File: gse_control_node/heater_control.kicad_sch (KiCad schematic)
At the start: 2 parts, among them J11 Conn_02x02_Counter_Clockwise, J12 Conn_02x04_Counter_Clockwise

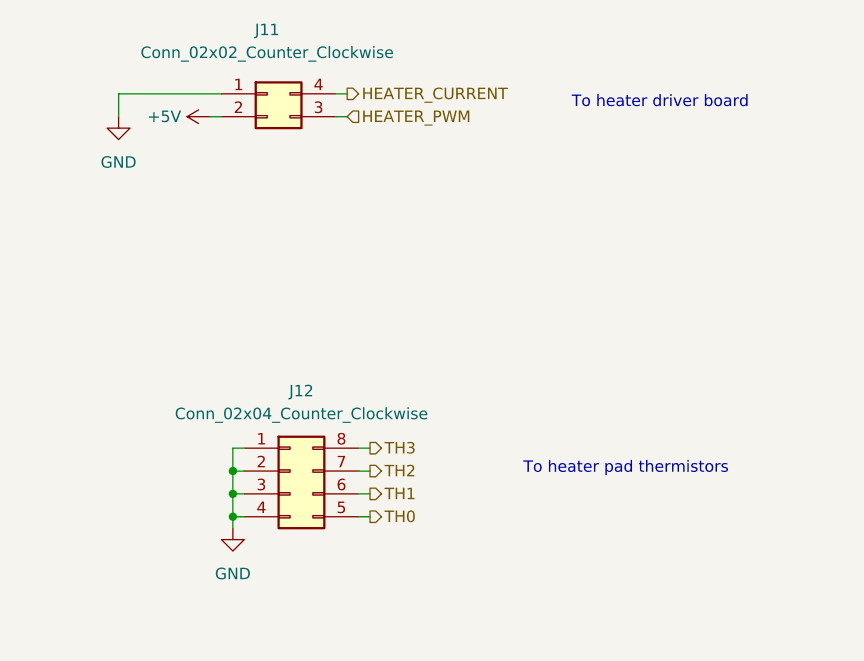
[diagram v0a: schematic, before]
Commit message: finish control board routing
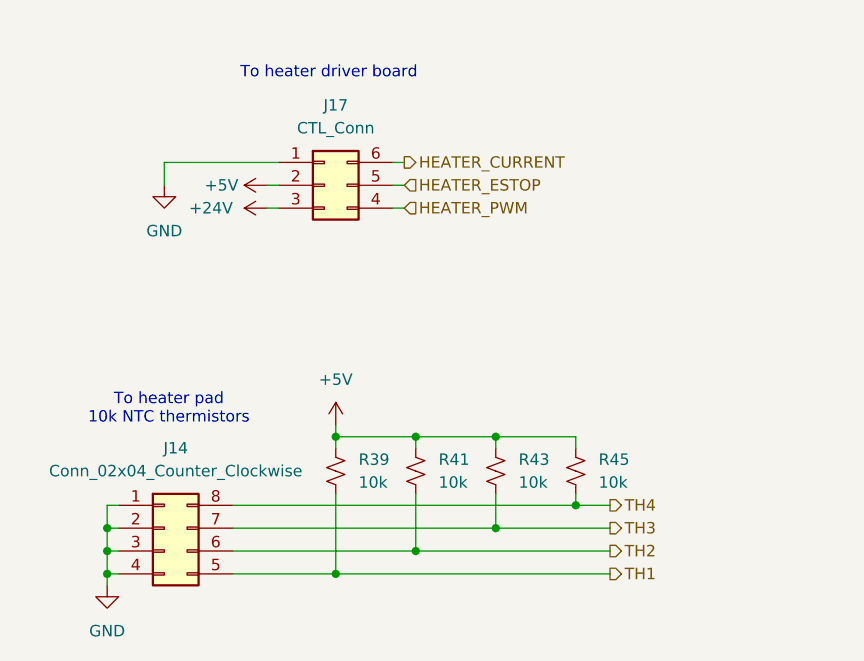
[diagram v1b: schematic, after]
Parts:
- removed J11: Conn_02x02_Counter_Clockwise, Connector_Molex:Molex_Micro-Fit_3.0_43045-0412_2x02_P3.00mm_Vertical, symbol Connector_Generic:Conn_02x02_Counter_Clockwise
- added J17: CTL_Conn, Connector_Molex:Molex_Micro-Fit_3.0_43045-0612_2x03_P3.00mm_Vertical, symbol Connector_Generic:Conn_02x03_Counter_Clockwise
- added R39, R41, R43, R45: 10k, Resistor_SMD:R_0603_1608Metric, symbol Device:R_Small_US
- renumbered J12 to J14
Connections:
- net TH0 is gone; now on net TH1: J14.5 (Pin_5)
- net +5V: now also J17.2 (Pin_2), R39.1, R41.1, R43.1, R45.1
- net GND: now also J17.1 (Pin_1)
- net HEATER_CURRENT: now also J17.6 (Pin_6)
- net HEATER_PWM: now also J17.4 (Pin_4)
- net TH1: now also R39.2; no longer J14.6 (Pin_6)
- net TH2: now also J14.6 (Pin_6), R41.2; no longer J14.7 (Pin_7)
- net TH3: now also J14.7 (Pin_7), R43.2; no longer J14.8 (Pin_8)
- new net +24V: J17.3 (Pin_3)
- new net HEATER_ESTOP: J17.5 (Pin_5)
- new net TH4: J14.8 (Pin_8), R45.2
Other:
- note added: "To heater pad 10k NTC thermistors"
- note removed: "To heater pad thermistors"
- moved on the sheet: J14

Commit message: updates for manufacturing
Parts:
- R39, R41, R43, R45: value 10k -> 10k 0.1%
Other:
- moved on the sheet: R41, R43, R45
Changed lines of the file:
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@@
+	)
+	(junction
+		(at 135.89 129.54)
+		(diameter 0)
+		(color 0 0 0 0)
 	)
 	(junction
@@
 	)
 	(junction
-		(at 153.67 124.46)
-		(diameter 0)
-		(color 0 0 0 0)
-	)
-	(junction
-		(at 144.78 127)
+		(at 148.59 127)
 		(diameter 0)
 		(color 0 0 0 0)
@@
 	)
 	(junction
-		(at 153.67 114.3)
-		(diameter 0)
-		(color 0 0 0 0)
-	)
-	(junction
-		(at 162.56 121.92)
+		(at 161.29 124.46)
 		(diameter 0)
 		(color 0 0 0 0)
@@
 	)
 	(junction
-		(at 144.78 114.3)
-		(diameter 0)
-		(color 0 0 0 0)
-	)
-	(junction
-		(at 135.89 129.54)
-		(diameter 0)
-		(color 0 0 0 0)
-	)
-	(junction
 		(at 110.49 124.46)
 		(diameter 0)
 		(color 0 0 0 0)
 	)
-	(wire
-		(pts
-			(xy 144.78 120.65) (xy 144.78 127)
-		)
-		(stroke
-			(width 0)
-			(type default)
-		)
-	)
-	(wire
-		(pts
-			(xy 162.56 121.92) (xy 166.37 121.92)
+	(junction
+		(at 173.99 121.92)
+		(diameter 0)
+		(color 0 0 0 0)
+	)
+	(junction
+		(at 161.29 114.3)
+		(diameter 0)
+		(color 0 0 0 0)
+	)
+	(junction
+		(at 148.59 114.3)
+		(diameter 0)
+		(color 0 0 0 0)
+	)
+	(wire
+		(pts
+			(xy 148.59 120.65) (xy 148.59 127)
 		)
 		(stroke
@@
 	(wire
 		(pts
-			(xy 153.67 124.46) (xy 166.37 124.46)
-		)
-		(stroke
-			(width 0)
-			(type default)
-		)
-	)
-	(wire
-		(pts
 			(xy 110.49 124.46) (xy 110.49 121.92)
 		)
@@
 	(wire
 		(pts
-			(xy 153.67 114.3) (xy 144.78 114.3)
+			(xy 148.59 114.3) (xy 161.29 114.3)
 		)
 		(stroke
@@
 	(wire
 		(pts
-			(xy 124.46 127) (xy 144.78 127)
-		)
-		(stroke
-			(width 0)
-			(type default)
-		)
-	)
-	(wire
-		(pts
-			(xy 162.56 115.57) (xy 162.56 114.3)
+			(xy 124.46 127) (xy 148.59 127)
+		)
+		(stroke
+			(width 0)
+			(type default)
+		)
+	)
+	(wire
+		(pts
+			(xy 173.99 115.57) (xy 173.99 114.3)
 		)
 		(stroke
@@
 	(wire
 		(pts
-			(xy 162.56 120.65) (xy 162.56 121.92)
+			(xy 173.99 120.65) (xy 173.99 121.92)
 		)
 		(stroke
@@
 	(wire
 		(pts
-			(xy 124.46 124.46) (xy 153.67 124.46)
+			(xy 173.99 121.92) (xy 186.69 121.92)
+		)
+		(stroke
+			(width 0)
+			(type default)
+		)
+	)
+	(wire
+		(pts
+			(xy 124.46 124.46) (xy 161.29 124.46)
 		)
 		(stroke
@@
 	(wire
 		(pts
-			(xy 144.78 127) (xy 166.37 127)
-		)
-		(stroke
-			(width 0)
-			(type default)
-		)
-	)
-	(wire
-		(pts
-			(xy 153.67 115.57) (xy 153.67 114.3)
+			(xy 161.29 115.57) (xy 161.29 114.3)
 		)
 		(stroke
@@
 	(wire
 		(pts
+			(xy 161.29 124.46) (xy 186.69 124.46)
+		)
+		(stroke
+			(width 0)
+			(type default)
+		)
+	)
+	(wire
+		(pts
 			(xy 142.24 88.9) (xy 143.51 88.9)
 		)
@@
 	(wire
 		(pts
+			(xy 135.89 129.54) (xy 186.69 129.54)
+		)
+		(stroke
+			(width 0)
+			(type default)
+		)
+	)
+	(wire
+		(pts
 			(xy 128.27 86.36) (xy 129.54 86.36)
 		)
@@
 	(wire
 		(pts
-			(xy 135.89 129.54) (xy 166.37 129.54)
-		)
-		(stroke
-			(width 0)
-			(type default)
-		)
-	)
-	(wire
-		(pts
 			(xy 124.46 129.54) (xy 135.89 129.54)
 		)
@@
 	(wire
 		(pts
+			(xy 148.59 127) (xy 186.69 127)
+		)
+		(stroke
+			(width 0)
+			(type default)
+		)
+	)
+	(wire
+		(pts
 			(xy 116.84 83.82) (xy 129.54 83.82)
 		)
@@
 	(wire
 		(pts
-			(xy 162.56 114.3) (xy 153.67 114.3)
-		)
-		(stroke
-			(width 0)
-			(type default)
-		)
-	)
-	(wire
-		(pts
-			(xy 124.46 121.92) (xy 162.56 121.92)
-		)
-		(stroke
-			(width 0)
-			(type default)
-		)
-	)
-	(wire
-		(pts
-			(xy 144.78 115.57) (xy 144.78 114.3)
-		)
-		(stroke
-			(width 0)
-			(type default)
-		)
-	)
-	(wire
-		(pts
-			(xy 144.78 114.3) (xy 135.89 114.3)
-		)
-		(stroke
-			(width 0)
-			(type default)
-		)
-	)
-	(wire
-		(pts
-			(xy 153.67 120.65) (xy 153.67 124.46)
+			(xy 173.99 114.3) (xy 161.29 114.3)
+		)
+		(stroke
+			(width 0)
+			(type default)
+		)
+	)
+	(wire
+		(pts
+			(xy 124.46 121.92) (xy 173.99 121.92)
+		)
+		(stroke
+			(width 0)
+			(type default)
+		)
+	)
+	(wire
+		(pts
+			(xy 148.59 115.57) (xy 148.59 114.3)
+		)
+		(stroke
+			(width 0)
+			(type default)
+		)
+	)
+	(wire
+		(pts
+			(xy 135.89 114.3) (xy 148.59 114.3)
+		)
+		(stroke
+			(width 0)
+			(type default)
+		)
+	)
+	(wire
+		(pts
+			(xy 161.29 120.65) (xy 161.29 124.46)
 		)
 		(stroke
@@
 	(hierarchical_label "TH2"
 		(shape output)
-		(at 166.37 127 0)
+		(at 186.69 127 0)
 		(effects
 			(font
@@
 	(hierarchical_label "TH4"
 		(shape output)
-		(at 166.37 121.92 0)
+		(at 186.69 121.92 0)
 		(effects
 			(font
@@
 	(hierarchical_label "TH1"
 		(shape output)
-		(at 166.37 129.54 0)
+		(at 186.69 129.54 0)
 		(effects
 			(font
@@
 	(hierarchical_label "TH3"
 		(shape output)
-		(at 166.37 124.46 0)
+		(at 186.69 124.46 0)
 		(effects
 			(font
@@
 			)
 		)
-		(property "Value" "10k"
+		(property "Value" "10k 0.1%"
 			(at 138.43 119.3799 0)
 			(show_name no)
@@
 	(symbol
 		(lib_id "Device:R_Small_US")
-		(at 162.56 118.11 0)
+		(at 173.99 118.11 0)
 		(unit 1)
 		(body_style 1)
@@
 		(fields_autoplaced yes)
 		(property "Reference" "R45"
-			(at 165.1 116.8399 0)
+			(at 176.53 116.8399 0)
 			(show_name no)
 			(do_not_autoplace no)
@@
 			)
 		)
-		(property "Value" "10k"
-			(at 165.1 119.3799 0)
+		(property "Value" "10k 0.1%"
+			(at 176.53 119.3799 0)
 			(show_name no)
 			(do_not_autoplace no)
@@
 		)
 		(property "Footprint" "Resistor_SMD:R_0603_1608Metric"
-			(at 162.56 118.11 0)
+			(at 173.99 118.11 0)
 			(hide yes)
 			(show_name no)
@@
 		)
 		(property "Datasheet" ""
-			(at 162.56 118.11 0)
+			(at 173.99 118.11 0)
 			(hide yes)
 			(show_name no)
@@
 		)
 		(property "Description" "Resistor, small US symbol"
-			(at 162.56 118.11 0)
+			(at 173.99 118.11 0)
 			(hide yes)
 			(show_name no)
@@
 	(symbol
 		(lib_id "Device:R_Small_US")
-		(at 144.78 118.11 0)
+		(at 148.59 118.11 0)
 		(unit 1)
 		(body_style 1)
@@
 		(fields_autoplaced yes)
 		(property "Reference" "R41"
-			(at 147.32 116.8399 0)
+			(at 151.13 116.8399 0)
 			(show_name no)
 			(do_not_autoplace no)
@@
 			)
 		)
-		(property "Value" "10k"
-			(at 147.32 119.3799 0)
+		(property "Value" "10k 0.1%"
+			(at 151.13 119.3799 0)
 			(show_name no)
 			(do_not_autoplace no)
@@
 		)
 		(property "Footprint" "Resistor_SMD:R_0603_1608Metric"
-			(at 144.78 118.11 0)
+			(at 148.59 118.11 0)
 			(hide yes)
 			(show_name no)
@@
 		)
 		(property "Datasheet" ""
-			(at 144.78 118.11 0)
+			(at 148.59 118.11 0)
 			(hide yes)
 			(show_name no)
@@
 		)
 		(property "Description" "Resistor, small US symbol"
-			(at 144.78 118.11 0)
+			(at 148.59 118.11 0)
 			(hide yes)
 			(show_name no)
@@
 	(symbol
 		(lib_id "Device:R_Small_US")
-		(at 153.67 118.11 0)
+		(at 161.29 118.11 0)
 		(unit 1)
 		(body_style 1)
@@
 		(fields_autoplaced yes)
 		(property "Reference" "R43"
-			(at 156.21 116.8399 0)
+			(at 163.83 116.8399 0)
 			(show_name no)
 			(do_not_autoplace no)
@@
 			)
 		)
-		(property "Value" "10k"
-			(at 156.21 119.3799 0)
+		(property "Value" "10k 0.1%"
+			(at 163.83 119.3799 0)
 			(show_name no)
 			(do_not_autoplace no)
@@
 		)
 		(property "Footprint" "Resistor_SMD:R_0603_1608Metric"
-			(at 153.67 118.11 0)
+			(at 161.29 118.11 0)
 			(hide yes)
 			(show_name no)
@@
 		)
 		(property "Datasheet" ""
-			(at 153.67 118.11 0)
+			(at 161.29 118.11 0)
 			(hide yes)
 			(show_name no)
@@
 		)
 		(property "Description" "Resistor, small US symbol"
-			(at 153.67 118.11 0)
-			(hide yes)
-			(show_name no)
+			(at 161.29 118.11 0)
+			(hide yes)
+			(show_name no)
